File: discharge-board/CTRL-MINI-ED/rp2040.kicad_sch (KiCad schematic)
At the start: 19 parts, among them U5 RP2040, U6 W25Q128JVS, Y1 12MHz

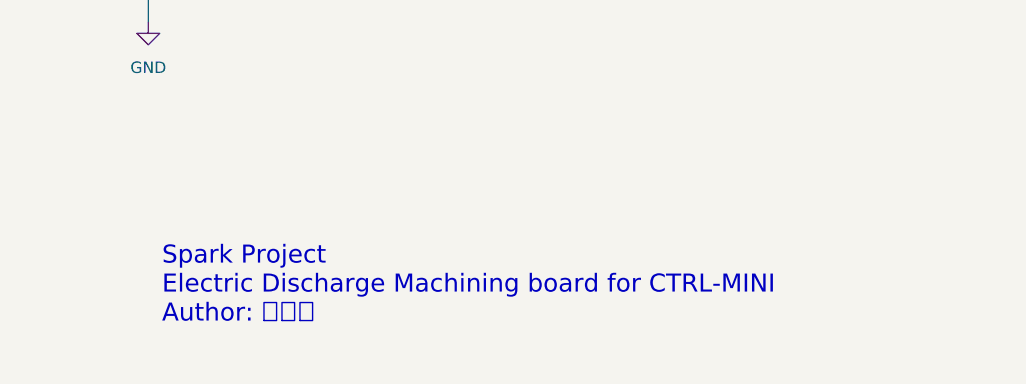
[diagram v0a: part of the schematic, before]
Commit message: Add PWM voltage divider and refactor
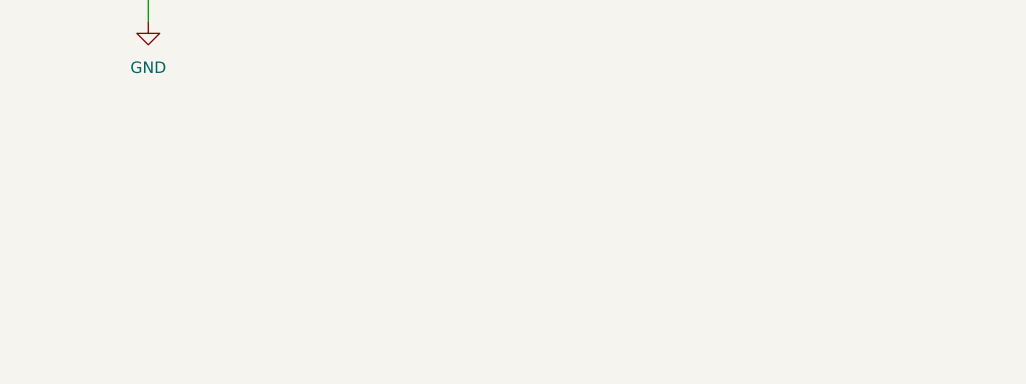
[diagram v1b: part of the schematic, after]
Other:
- note removed: "Spark Project Electric Discharge Machining board for CTRL-MINI Author: 夕月霞"
- company: (none) -> Spark Project
- title: (none) -> CTRL-MINI-ED
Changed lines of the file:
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@@
 	(generator_version "8.0")
 	(paper "A4")
+	(title_block
+		(title "CTRL-MINI-ED")
+		(date "2024-12-11")
+		(rev "2")
+		(company "Spark Project")
+		(comment 1 "Author: 夕月霞 (xyx)")
+		(comment 2 "Electric Discharge Machining board for CTRL-MINI")
+	)
 	(junction
 		(at 63.5 152.4)
@@
 	)
 	(image
-		(at 184.15 173.99)
+		(at 276.86 173.99)
+		(scale 1.13867)
 		(data "iVBORw0KGgoAAAANSUhEUgAAATsAAAEsCAYAAAC8DxTkAAAACXBIWXMAAHc0AAB3NAG21TCYAAAA"
 			"GXRFWHRTb2Z0d2FyZQB3d3cuaW5rc2NhcGUub3Jnm+48GgAAIABJREFUeJzt3XmcXFWZ//HPc6u6"
@@
 		)
 	)
-	(text "Spark Project\nElectric Discharge Machining board for CTRL-MINI\nAuthor: 夕月霞"
-		(exclude_from_sim yes)
-		(at 192.024 169.672 0)
-		(effects
-			(font
-				(size 2 2)
-				(color 132 0 0 1)
-			)
-			(justify left top)
-		)
-	)
